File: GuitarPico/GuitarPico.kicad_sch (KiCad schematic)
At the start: 112 parts, among them J1 INPUT, J2 INPUT, J3 OUTPUT, J4 OUTPUT, J5 Barrel_Jack_Switch, J8 INPUT, J9 INPUT, Q1 2N3904, Q2 2N3904, Q3 2N3904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

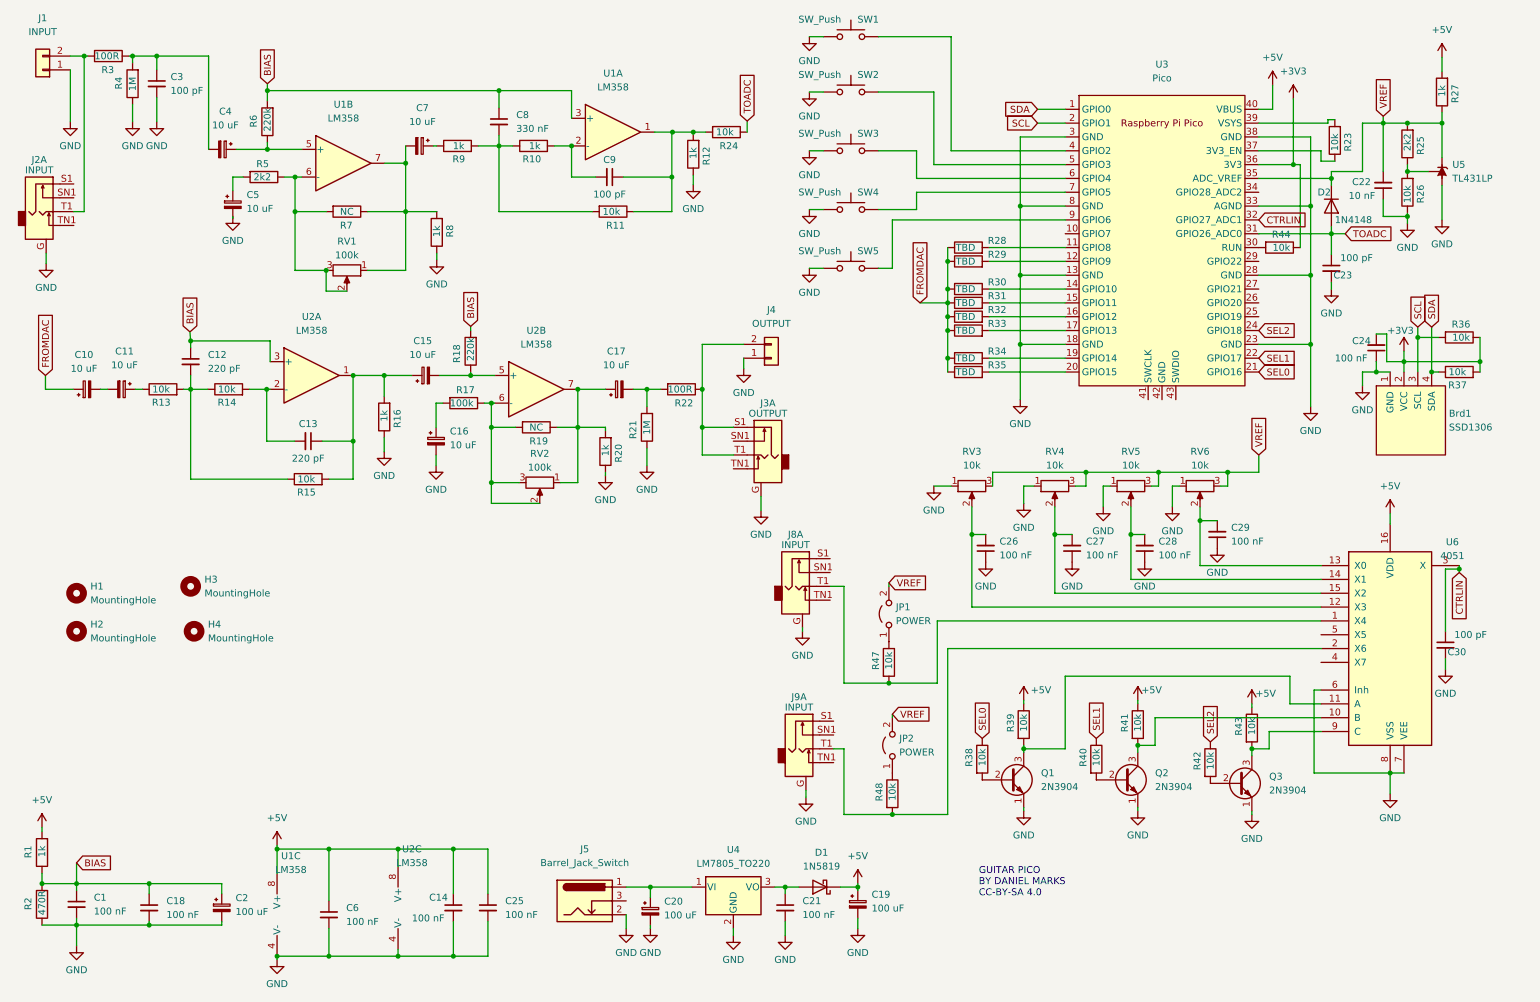
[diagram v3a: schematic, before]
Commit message: Added VGA connector!
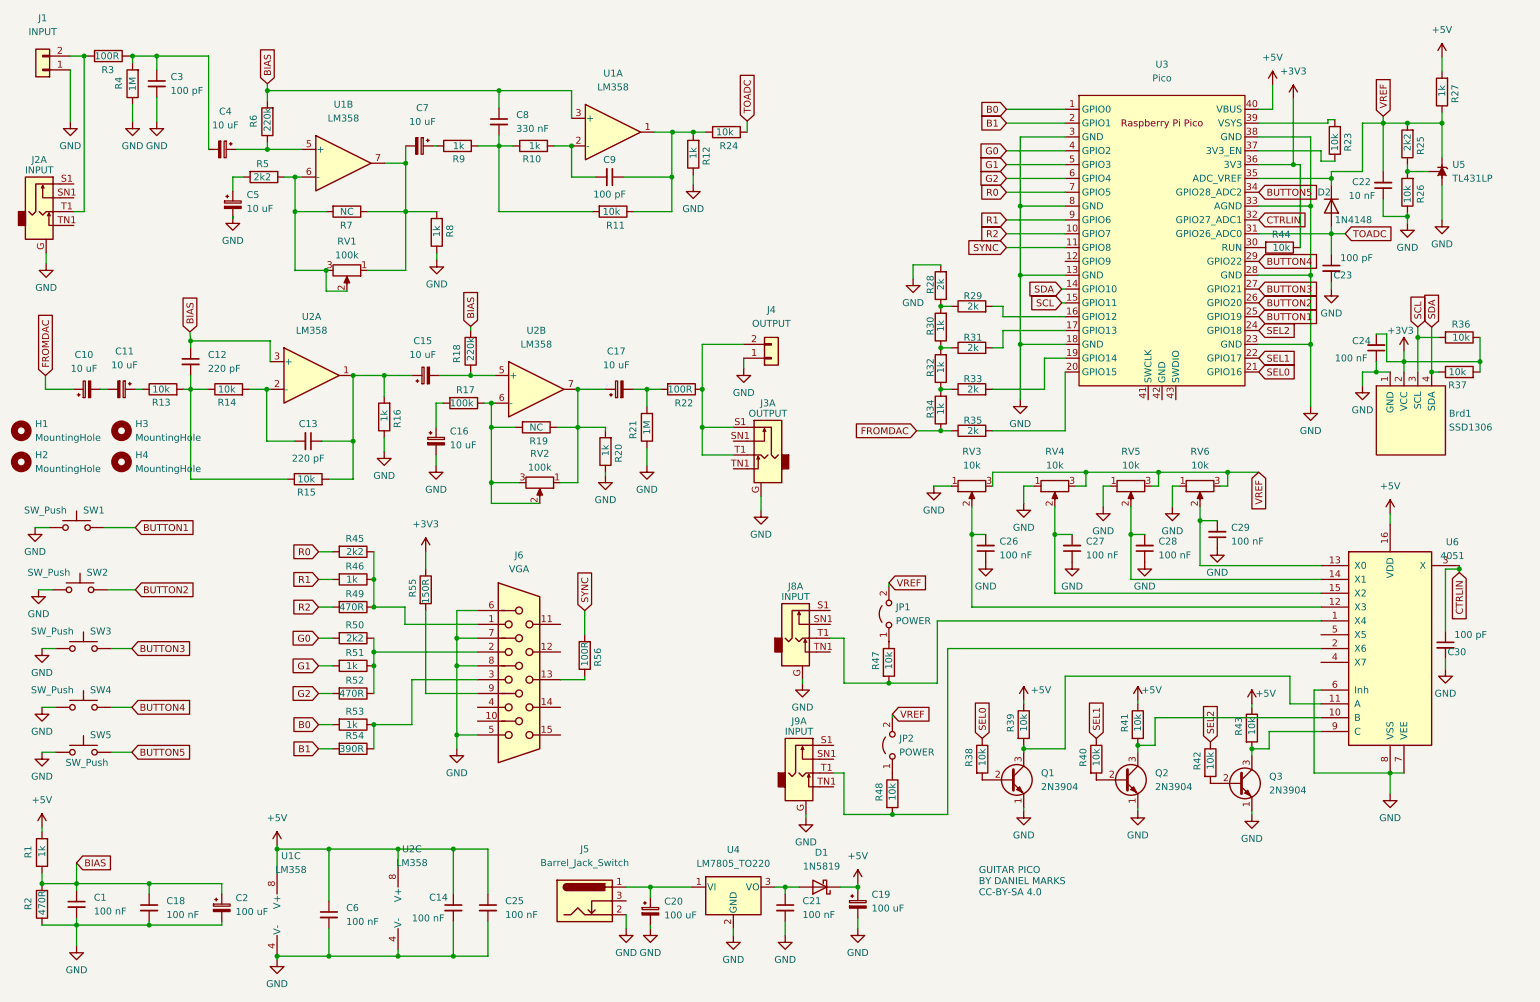
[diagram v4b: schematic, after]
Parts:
- added J6: VGA, Connector_Dsub:DSUB-15-HD_Female_Horizontal_P2.29x1.98mm_EdgePinOffset3.03mm_Housed_MountingHolesOffset4.94mm, symbol Connector:DB15_Female_HighDensity
- added R45, R50: 2k2, Resistor_THT:R_Axial_DIN0207_L6.3mm_D2.5mm_P7.62mm_Horizontal, symbol Device:R
- added R46, R51, R53: 1k, Resistor_THT:R_Axial_DIN0207_L6.3mm_D2.5mm_P7.62mm_Horizontal, symbol Device:R
- added R49, R52: 470R, Resistor_THT:R_Axial_DIN0207_L6.3mm_D2.5mm_P7.62mm_Horizontal, symbol Device:R
- added R54: 390R, Resistor_THT:R_Axial_DIN0207_L6.3mm_D2.5mm_P7.62mm_Horizontal, symbol Device:R
- added R55: 150R, Resistor_THT:R_Axial_DIN0207_L6.3mm_D2.5mm_P7.62mm_Horizontal, symbol Device:R
- added R56: 100R, Resistor_THT:R_Axial_DIN0207_L6.3mm_D2.5mm_P7.62mm_Horizontal, symbol Device:R
- R28: renamed from R31; value TBD -> 2k
- R29: renamed from R28; value TBD -> 2k
- R30: renamed from R34; value TBD -> 1k
- R31: renamed from R33; value TBD -> 2k
- R32: renamed from R35; value TBD -> 1k
- R33: renamed from R29; value TBD -> 2k
- R34: renamed from R30; value TBD -> 1k
- R35: renamed from R32; value TBD -> 2k
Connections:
- net +3V3: now also R55.1
- net FROMDAC: no longer R28.1, R29.1, R30.1, R31.1, R32.1, R33.1
- net GND: now also R28.2, J6.5, J6.6, J6.7, J6.8
- net SCL: now also U3.15 (GPIO11); no longer U3.2 (GPIO1)
- net SDA: now also U3.14 (GPIO10); no longer U3.1 (GPIO0)
- net at R32.2: now also R30.1, R31.1; no longer U3.20 (GPIO15)
- net at R29.2: now also U3.16 (GPIO12); no longer U3.11 (GPIO8)
- net at R35.2: now also U3.20 (GPIO15); no longer U3.16 (GPIO12)
- net at R34.2: now also R32.1, R33.1; no longer U3.14 (GPIO10)
- net R2: now reaches U3.10 (GPIO7)
- net R2: now also R49.2
- net at U3.12 (GPIO9): no longer R33.2
- net at R30.2: now also R28.1, R29.1; no longer U3.19 (GPIO14)
- net BUTTON1: now reaches U3.25 (GPIO19)
- net BUTTON1: now also SW1.2
- net BUTTON2: now reaches U3.26 (GPIO20)
- net BUTTON2: now also SW2.2
- net BUTTON3: now reaches U3.27 (GPIO21)
- net BUTTON3: now also SW3.2
- net BUTTON4: now reaches U3.29 (GPIO22)
- net BUTTON4: now also SW4.2
- net BUTTON5: now reaches U3.34 (GPIO28_ADC2)
- net BUTTON5: now also SW5.2
- net G0: now reaches U3.4 (GPIO2)
- net G0: now also R50.2; no longer SW1.2
- net G1: now reaches U3.5 (GPIO3)
- net G1: now also R51.2; no longer SW2.2
- net G2: now reaches U3.6 (GPIO4)
- net G2: now also R52.2; no longer SW3.2
- net R0: now reaches U3.7 (GPIO5)
- net R0: now also R45.2; no longer SW4.2
- net R1: now reaches U3.9 (GPIO6)
- net R1: now also R46.2; no longer SW5.2
- new net: J6.1, R45.1, R46.1, R49.1
- new net: J6.13, R56.1
- new net: J6.2, R50.1, R51.1, R52.1
- new net: J6.3, R53.1, R54.1
- new net: J6.9, R55.2
- new net: R33.2, U3.19 (GPIO14)
- new net B0: R53.2, U3.1 (GPIO0)
- new net B1: R54.2, U3.2 (GPIO1)
- new net SYNC: R56.2, U3.11 (GPIO8)
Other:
- moved on the sheet: H1, H2, H3, H4, J8A, J9A, R28, R29, R30, R31, R32, R33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

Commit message: Added CAD pedal
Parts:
- added C31: 10 nF, Capacitor_THT:C_Disc_D5.0mm_W2.5mm_P5.00mm, symbol Device:C_Small
- added R57: 100R, Resistor_THT:R_Axial_DIN0207_L6.3mm_D2.5mm_P7.62mm_Horizontal, symbol Device:R
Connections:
- net GND: now also C31.1
- net VREF: now also C31.2
- net at J6.14: now also R57.1
- net VSYNC: now reaches U3.12 (GPIO9)
- net VSYNC: now also R57.2
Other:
- moved on the sheet: C22, R25, R26, R27, U5

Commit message: Added simulations
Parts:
- C12: value 220 pF -> 2200 pF
- C13: value 220 pF -> 470 pF
- C8: value 330 nF -> 2200 pF
- C9: value 100 pF -> 47 pF
- R10, R9: value 1k -> 10k
- R11: value 10k -> 100k
- R13: value 10k -> 220k
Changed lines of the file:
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@@
       (effects (font (size 1.27 1.27)) (justify left))
     )
-    (property "Value" "10k" (id 1) (at 122.047 49.911 90)
+    (property "Value" "100k" (id 1) (at 121.92 50.165 90)
       (effects (font (size 1.27 1.27)) (justify left))
     )
@@
     (in_bom yes) (on_board yes)
     (property "Reference" "C9" (id 0) (at 123.317 40.386 90))
-    (property "Value" "100 pF" (id 1) (at 123.317 46.736 90))
+    (property "Value" "47 pF" (id 1) (at 123.317 46.736 90))
     (property "Footprint" "Capacitor_THT:C_Disc_D5.0mm_W2.5mm_P5.00mm" (id 2) (at 123.317 43.561 0)
       (effects (font (size 1.27 1.27)) hide)
@@
       (effects (font (size 1.27 1.27)) (justify left))
     )
-    (property "Value" "1k" (id 1) (at 110.617 37.846 90)
+    (property "Value" "10k" (id 1) (at 110.617 37.846 90)
       (effects (font (size 1.27 1.27)) (justify left))
     )
@@
       (effects (font (size 1.27 1.27)) (justify left))
     )
-    (property "Value" "10k" (id 1) (at 42.545 82.55 90)
+    (property "Value" "220k" (id 1) (at 43.815 82.55 90)
       (effects (font (size 1.27 1.27)) (justify left))
     )
@@
   (symbol (lib_id "Device:C_Small") (at 102.997 33.401 0) (unit 1)
     (in_bom yes) (on_board yes) (fields_autoplaced)
-    (property "Reference" "C8" (id 0) (at 106.172 32.1372 0)
+    (property "Reference" "C8" (id 0) (at 105.41 32.1372 0)
       (effects (font (size 1.27 1.27)) (justify left))
     )
-    (property "Value" "330 nF" (id 1) (at 106.172 34.6772 0)
+    (property "Value" "2200 pF" (id 1) (at 105.41 34.6772 0)
       (effects (font (size 1.27 1.27)) (justify left))
     )
@@
       (effects (font (size 1.27 1.27)) (justify left))
     )
-    (property "Value" "220 pF" (id 1) (at 49.53 78.7462 0)
+    (property "Value" "2200 pF" (id 1) (at 49.53 78.7462 0)
       (effects (font (size 1.27 1.27)) (justify left))
     )
@@
   (symbol (lib_id "Device:R") (at 109.855 89.535 270) (unit 1)
     (in_bom yes) (on_board yes)
-    (property "Reference" "R19" (id 0) (at 108.585 92.075 90)
+    (property "Reference" "R19" (id 0) (at 108.585 86.995 90)
       (effects (font (size 1.27 1.27)) (justify left))
     )
@@
       (effects (font (size 1.27 1.27)) (justify left))
     )
-    (property "Value" "1k" (id 1) (at 96.647 37.846 90)
+    (property "Value" "10k" (id 1) (at 96.647 37.846 90)
       (effects (font (size 1.27 1.27)) (justify left))
     )
@@
     (in_bom yes) (on_board yes)
     (property "Reference" "C13" (id 0) (at 67.945 88.9 90))
-    (property "Value" "220 pF" (id 1) (at 67.945 95.25 90))
+    (property "Value" "470 pF" (id 1) (at 67.945 95.25 90))
     (property "Footprint" "Capacitor_THT:C_Disc_D5.0mm_W2.5mm_P5.00mm" (id 2) (at 67.945 92.075 0)
       (effects (font (size 1.27 1.27)) hide)
@@
     )
     (path "/7c8415b8-7547-4704-bf1c-41e45abebbf6"
-      (reference "C8") (unit 1) (value "330 nF") (footprint "Capacitor_THT:C_Disc_D5.0mm_W2.5mm_P5.00mm")
+      (reference "C8") (unit 1) (value "2200 pF") (footprint "Capacitor_THT:C_Disc_D5.0mm_W2.5mm_P5.00mm")
     )
     (path "/1d2e8b1f-46b0-47a7-a4b5-d2612d2633f0"
-      (reference "C9") (unit 1) (value "100 pF") (footprint "Capacitor_THT:C_Disc_D5.0mm_W2.5mm_P5.00mm")
+      (reference "C9") (unit 1) (value "47 pF") (footprint "Capacitor_THT:C_Disc_D5.0mm_W2.5mm_P5.00mm")
     )
     (path "/2e8ce526-6fc8-4bf6-8e88-01110c5fb478"
@@
     )
     (path "/944a30cb-00bd-425f-b8d2-7613a7bc143d"
-      (reference "C12") (unit 1) (value "220 pF") (footprint "Capacitor_THT:C_Disc_D5.0mm_W2.5mm_P5.00mm")
+      (reference "C12") (unit 1) (value "2200 pF") (footprint "Capacitor_THT:C_Disc_D5.0mm_W2.5mm_P5.00mm")
     )
     (path "/f9e582af-f7a7-46da-b838-4d87800ad119"
-      (reference "C13") (unit 1) (value "220 pF") (footprint "Capacitor_THT:C_Disc_D5.0mm_W2.5mm_P5.00mm")
+      (reference "C13") (unit 1) (value "470 pF") (footprint "Capacitor_THT:C_Disc_D5.0mm_W2.5mm_P5.00mm")
     )
     (path "/7b62232e-dc1b-424a-bd96-df5531b112a2"
@@
     )
     (path "/d4beb8d8-4bc5-47e7-9fb4-402e9c122e28"
-      (reference "R9") (unit 1) (value "1k") (footprint "Resistor_THT:R_Axial_DIN0207_L6.3mm_D2.5mm_P7.62mm_Horizontal")
+      (reference "R9") (unit 1) (value "10k") (footprint "Resistor_THT:R_Axial_DIN0207_L6.3mm_D2.5mm_P7.62mm_Horizontal")
     )
     (path "/34f11cdf-c071-4cc5-a787-48df288af0ba"
-      (reference "R10") (unit 1) (value "1k") (footprint "Resistor_THT:R_Axial_DIN0207_L6.3mm_D2.5mm_P7.62mm_Horizontal")
+      (reference "R10") (unit 1) (value "10k") (footprint "Resistor_THT:R_Axial_DIN0207_L6.3mm_D2.5mm_P7.62mm_Horizontal")
     )
     (path "/136aa926-be0e-4d47-8f5a-3e755b401e00"
-      (reference "R11") (unit 1) (value "10k") (footprint "Resistor_THT:R_Axial_DIN0207_L6.3mm_D2.5mm_P7.62mm_Horizontal")
+      (reference "R11") (unit 1) (value "100k") (footprint "Resistor_THT:R_Axial_DIN0207_L6.3mm_D2.5mm_P7.62mm_Horizontal")
     )
     (path "/9949ef93-2cf9-4b67-a871-53f2bebedd68"
@@
     )
     (path "/497e8e16-db24-4b63-b1a9-654c978540b6"
-      (reference "R13") (unit 1) (value "10k") (footprint "Resistor_THT:R_Axial_DIN0207_L6.3mm_D2.5mm_P7.62mm_Horizontal")
+      (reference "R13") (unit 1) (value "220k") (footprint "Resistor_THT:R_Axial_DIN0207_L6.3mm_D2.5mm_P7.62mm_Horizontal")
     )
     (path "/8311fdd2-488f-44b2-97f8-bec3fa3e522a"

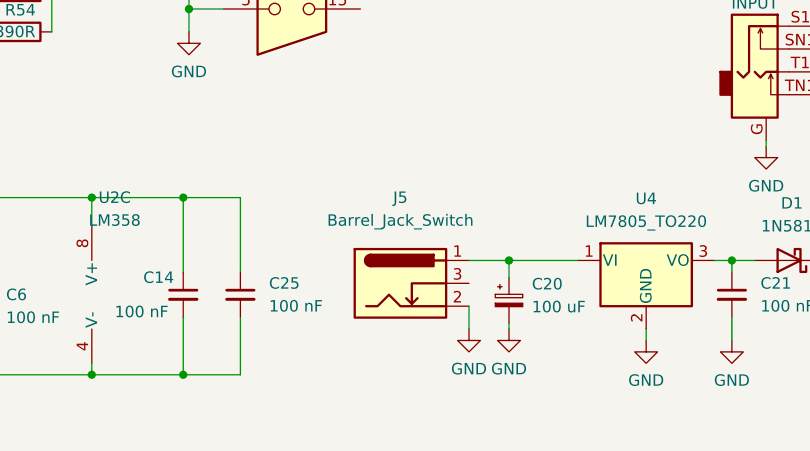
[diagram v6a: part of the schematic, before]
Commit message: Added FIR Filter examples
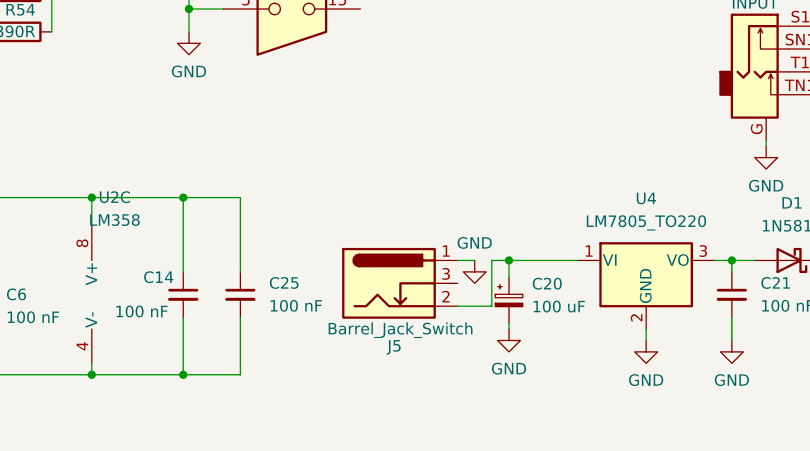
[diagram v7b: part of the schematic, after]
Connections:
- net GND: now also J5.1; no longer J5.2
- net at C20.1, U4.1 (VI): now also J5.2; no longer J5.1
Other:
- moved on the sheet: J5
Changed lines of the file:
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@@
   (junction (at 184.15 74.93) (diameter 0) (color 0 0 0 0)
   )
+  (junction (at 130.81 173.99) (diameter 0) (color 0 0 0 0)
+  )
   (junction (at 210.82 97.79) (diameter 0) (color 0 0 0 0)
   )
@@
   (junction (at 281.305 33.655) (diameter 0) (color 0 0 0 0)
   )
-  (junction (at 130.81 173.99) (diameter 0) (color 0 0 0 0)
-  )
   (junction (at 76.2 80.01) (diameter 0) (color 0 0 0 0)
   )
@@
     (stroke (width 0) (type default) (color 0 0 0 0))
   )
+  (wire (pts (xy 128.905 173.99) (xy 128.905 179.07))
+    (stroke (width 0) (type default) (color 0 0 0 0))
+  )
   (wire (pts (xy 117.475 82.55) (xy 117.475 89.535))
     (stroke (width 0) (type default) (color 0 0 0 0))
@@
     (stroke (width 0) (type default) (color 0 0 0 0))
   )
-  (wire (pts (xy 126.365 173.99) (xy 130.81 173.99))
-    (stroke (width 0) (type default) (color 0 0 0 0))
-  )
   (wire (pts (xy 92.075 80.01) (xy 97.79 80.01))
     (stroke (width 0) (type default) (color 0 0 0 0))
@@
     (stroke (width 0) (type default) (color 0 0 0 0))
   )
+  (wire (pts (xy 125.095 173.99) (xy 127 173.99))
+    (stroke (width 0) (type default) (color 0 0 0 0))
+  )
   (wire (pts (xy 168.91 173.355) (xy 168.91 173.99))
     (stroke (width 0) (type default) (color 0 0 0 0))
@@
     (stroke (width 0) (type default) (color 0 0 0 0))
   )
+  (wire (pts (xy 128.905 173.99) (xy 130.81 173.99))
+    (stroke (width 0) (type default) (color 0 0 0 0))
+  )
   (wire (pts (xy 31.115 119.38) (xy 36.195 119.38))
     (stroke (width 0) (type default) (color 0 0 0 0))
@@
     (stroke (width 0) (type default) (color 0 0 0 0))
   )
-  (wire (pts (xy 126.365 179.07) (xy 126.365 181.61))
-    (stroke (width 0) (type default) (color 0 0 0 0))
-  )
   (wire (pts (xy 231.775 114.935) (xy 254 114.935))
     (stroke (width 0) (type default) (color 0 0 0 0))
@@
   )
   (wire (pts (xy 196.215 38.735) (xy 207.01 38.735))
+    (stroke (width 0) (type default) (color 0 0 0 0))
+  )
+  (wire (pts (xy 125.095 179.07) (xy 128.905 179.07))
     (stroke (width 0) (type default) (color 0 0 0 0))
   )
@@
     )
   )
-  (symbol (lib_id "power:GND") (at 126.365 181.61 0) (unit 1)
-    (in_bom yes) (on_board yes) (fields_autoplaced)
-    (property "Reference" "#PWR0125" (id 0) (at 126.365 187.96 0)
-      (effects (font (size 1.27 1.27)) hide)
-    )
-    (property "Value" "GND" (id 1) (at 126.365 186.055 0))
-    (property "Footprint" "" (id 2) (at 126.365 181.61 0)
-      (effects (font (size 1.27 1.27)) hide)
-    )
-    (property "Datasheet" "" (id 3) (at 126.365 181.61 0)
+  (symbol (lib_id "power:GND") (at 127 173.99 0) (unit 1)
+    (in_bom yes) (on_board yes)
+    (property "Reference" "#PWR0125" (id 0) (at 127 180.34 0)
+      (effects (font (size 1.27 1.27)) hide)
+    )
+    (property "Value" "GND" (id 1) (at 127 172.085 0))
+    (property "Footprint" "" (id 2) (at 127 173.99 0)
+      (effects (font (size 1.27 1.27)) hide)
+    )
+    (property "Datasheet" "" (id 3) (at 127 173.99 0)
       (effects (font (size 1.27 1.27)) hide)
     )
@@
     (pin "8")
   )
-  (symbol (lib_id "Connector:Barrel_Jack_Switch") (at 118.745 176.53 0) (unit 1)
-    (in_bom yes) (on_board yes) (fields_autoplaced)
-    (property "Reference" "J5" (id 0) (at 118.745 167.005 0))
-    (property "Value" "Barrel_Jack_Switch" (id 1) (at 118.745 169.545 0))
-    (property "Footprint" "Connector_BarrelJack:BarrelJack_Horizontal" (id 2) (at 120.015 177.546 0)
-      (effects (font (size 1.27 1.27)) hide)
-    )
-    (property "Datasheet" "~" (id 3) (at 120.015 177.546 0)
-      (effects (font (size 1.27 1.27)) hide)
-    )
+  (symbol (lib_id "Connector:Barrel_Jack_Switch") (at 117.475 176.53 0) (unit 1)
+    (in_bom yes) (on_board yes)
+    (property "Reference" "J5" (id 0) (at 118.11 183.515 0))
+    (property "Value" "Barrel_Jack_Switch" (id 1) (at 118.745 181.61 0))
+    (property "Footprint" "Connector_BarrelJack:BarrelJack_Horizontal" (id 2) (at 118.745 177.546 0)
+      (effects (font (size 1.27 1.27)) hide)
+    )
+    (property "Datasheet" "~" (id 3) (at 118.745 177.546 0)
+      (effects (font (size 1.27 1.27)) hide)
+    )

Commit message: First example of guitarpico project
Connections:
- net at C9.1, R11.1, U1.1: now also R12.2, R24.2
